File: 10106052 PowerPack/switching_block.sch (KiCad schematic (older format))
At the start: 0 parts

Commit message: start to create switching block
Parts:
- added C1, C?: 100n, symbol Device:C
- added C10, C11, C12: 10n, symbol Device:C
- added D1, D7: SMA6J28A, symbol Device:D_Schottky
- added D15: BAT54CWT1G, symbol Device:D_x2_KCom_AAK
- added D2, D8: SP0502BAHTG, symbol Device:D_Schottky_x2_ACom_KKA
- added D? (x3): PMEG4005AEA, symbol Device:D
- added J1, J2, J3, J5, J6, J7: 811-S1-002-10-015101, symbol Connector:Conn_01x02_Male
- added J4, J8: GKS 913 305 230 A 15 02 S, symbol Connector:Conn_01x01_Male
- added Q? (x2), T2, T4: SUD50P06-15, symbol Device:Q_NMOS_GDS
- added R1, R10, R7, R? (x3): 10k, symbol Device:R
- added R12, R2, R? (x2): 15k, symbol Device:R
- added R13, R8, R? (x2): 22k, symbol Device:R
- added R14, R4: 1k, symbol Device:R
- added R15 (x2): 18k, symbol Device:R
- added R28: 66.5k, symbol Device:R
- added R29: 40.2k, symbol Device:R
- added R3, R?: 100k, symbol Device:R
- added R50, R51: 100, symbol Device:R
- added R57, R58: 0, symbol Device:R
- added R?: 0.015, symbol Device:R
- added T1, T12, T13, T3, T? (x2): 2N7002TA, symbol Device:Q_NMOS_GSD
- added U3: INA170, Package_SO:MSOP-8_3x3mm_P0.65mm, symbol 10106052_PowerPack:INA170
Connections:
- new net: D1.1 (K), D?.2 (A), J1.1 (Pin_1), J1.2 (Pin_2), R2.1, R3.1, T2.3 (S)
- new net: J2.1 (Pin_1), J2.2 (Pin_2), R50.2, R57.2
- new net: D15.2 (A), R4.1, R50.1, T12.3 (D)
- new net: D2.2 (K), R57.1
- new net: D15.1 (A), R14.1, R51.1, T13.3 (D)
- new net: D7.1 (K), D?.2 (A), J5.1 (Pin_1), J5.2 (Pin_2), Q?.3 (S), R?.1, R?.1
- new net: J6.1 (Pin_1), J6.2 (Pin_2), R51.2, R58.2
- new net: D8.2 (K), R58.1
- new net: R1.2, T1.3 (D)
- new net: R1.1, R2.2, T2.1 (G)
- new net: T2.2 (D), T4.2 (D)
- new net: R10.1, R12.2, T4.1 (G)
- new net: C11.1, Q?.3 (S), R12.1, R?.1, R?.1, T4.3 (S), U3.1 (V-IN), U3.8 (V+)
- new net: R10.2, T3.3 (D)
- new net: R?.2, T?.3 (D) (x2)
- new net: Q?.1 (G), R?.1, R?.2 (x2)
- new net: Q?.2 (D), Q?.2 (D)
- new net: R?.2, U3.2 (V+IN)
- new net: R28.1, U3.5 (ROS)
- new net +3.0VREF: C10.1, U3.3 (VREF)
- new net +5V: R14.2, R15.2, R15.2, R4.2
- new net +VDC_PERM: D?.1 (K), D?.1 (K), D?.1 (K)
- new net CHARG_BAT1: R13.2, T3.1 (G)
- new net CHARG_BAT2: R?.2, T?.1 (G)
- new net DISCH_BAT1: R8.2, T1.1 (G)
- new net DISCH_BAT2: R?.2, T?.1 (G)
- new net GND: D1.2 (A), D2.3 (A), D7.2 (A), D8.3 (A), J4.1 (Pin_1), J8.1 (Pin_1), R13.1, R8.1, R?.1, R?.1, T1.2 (S), T12.2 (S), T13.2 (S), T3.2 (S), T?.2 (S), T?.2 (S)
- new net GNDA: C1.2, C10.2, C11.2, C12.2, C?.2, R28.2, R29.2, R7.2, R?.2, U3.4 (GND)
- new net IBAT_MEAS: C12.1, R29.1, U3.6 (OUT)
- new net ID_BAT1: T12.1 (G)
- new net ID_BAT2: T13.1 (G)
- new net ID_BAT_READ: D15.3 (K)
- new net TEMP_BAT1: D2.1 (K), J3.1 (Pin_1), J3.2 (Pin_2), R15.1
- new net TEMP_BAT2: D8.1 (K), J7.1 (Pin_1), J7.2 (Pin_2), R15.1
- new net VBAT1_MEAS: C1.1, R3.2, R7.1
- new net VBAT2_MEAS: C?.1, R?.1, R?.2
- new net V_DC_CHARGER: D?.2 (A)
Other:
- note added: "+BAT1"
- note added: "+BAT2"
- note added: "-BAT1"
- note added: "-BAT2"
- note added: "ID_BAT1"
- note added: "ID_BAT2"
- note added: "Note: R24 - place as close as possible to U3"

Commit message: schematic done2
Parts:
- added C14: 100n, symbol Device:C
- added C8, C?: 100u, symbol Device:CP
- added D9: SMA6J28A, symbol Device:D_Schottky
- added F1: Fuse, symbol Device:Fuse
- added FL1: BNX002-11, symbol 10106052_PowerPack:BNX002-11
- added J9: 26-61-4020, symbol Connector:Conn_01x02_Male
- added J?: 43650-0229, symbol Connector:Conn_01x02_Male
- added NT1: Net-Tie_2, symbol Device:Net-Tie_2
- added R25: 0, symbol Device:R
- added R27: 100k, symbol Device:R
- added R30, R53, R56: 10k, symbol Device:R
- added R32: 470, symbol Device:R
- added R52: 22k, symbol Device:R
- added R54: 15k, symbol Device:R
- added R55: 47k, symbol Device:R
- added RL1: 41.52.9.024.0010, Relay_THT:Relay_DPDT_Finder_40.52, symbol Relay:FINDER-41.52
- added T14: SUD50P06-15, symbol Device:Q_NMOS_GDS
- added T15: 2N7002TA, symbol Device:Q_NMOS_GSD
- gave numbers to parts that had none: 17
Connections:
- net GND: now also C8.2, C?.2, D9.2 (A), J9.2 (Pin_2), NT1.1, R52.1, R56.1, RL1.11, RL1.A2, T15.2 (S)
- net GNDA: now also C14.2, NT1.2, R30.2
- net V_DC_CHARGER: now also R25.1, R32.1
- net at R24.2, U3.2 (V+IN): now also C8.1, C?.1, R54.2, RL1.21, T14.3 (S)
- new net: FL1.1, RL1.22
- new net: FL1.2, J?.1 (Pin_1)
- new net: FL1.3, RL1.12
- new net: FL1.4, J?.2 (Pin_2)
- new net: R32.2, RL1.A1
- new net: R53.2, R54.1, T14.1 (G)
- new net: D9.1 (K), F1.1, R25.2, R27.1, R55.2, T14.2 (D)
- new net: R52.2, R55.1, R56.2, T15.1 (G)
- new net: R53.1, T15.3 (D)
- new net: F1.2, J9.1 (Pin_1)
- new net V_CH: C14.1, R27.2, R30.1
- no-connect marks 0 -> 2
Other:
- note added: "Charger DC"
- note added: "Internal battery"
- note added: "Note: J1 - J4 - TH components, place on Top side as marked;"
- note added: "Note: J5 - J8 - TH components, place on Top side as marked;"
- note added: "Note: J9 - TH component, place on Top right side;"
- note added: "Note: Join GND and AGND planes/traces;"
- note added: "Note: Power tracks (min 0.6mm, min 3.3A)\n - route as wide as possible;"
- note added: "Note: RL1, FL1 & J11 - TH components, place on Top right side;"
- note added: "Removable battery"
- note added: "TEMP_BAT1"
- note added: "TEMP_BAT2"
- moved on the sheet: C1, C10, C11, C12, C4, D1, D15, D2, D3, D4, D6, D7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

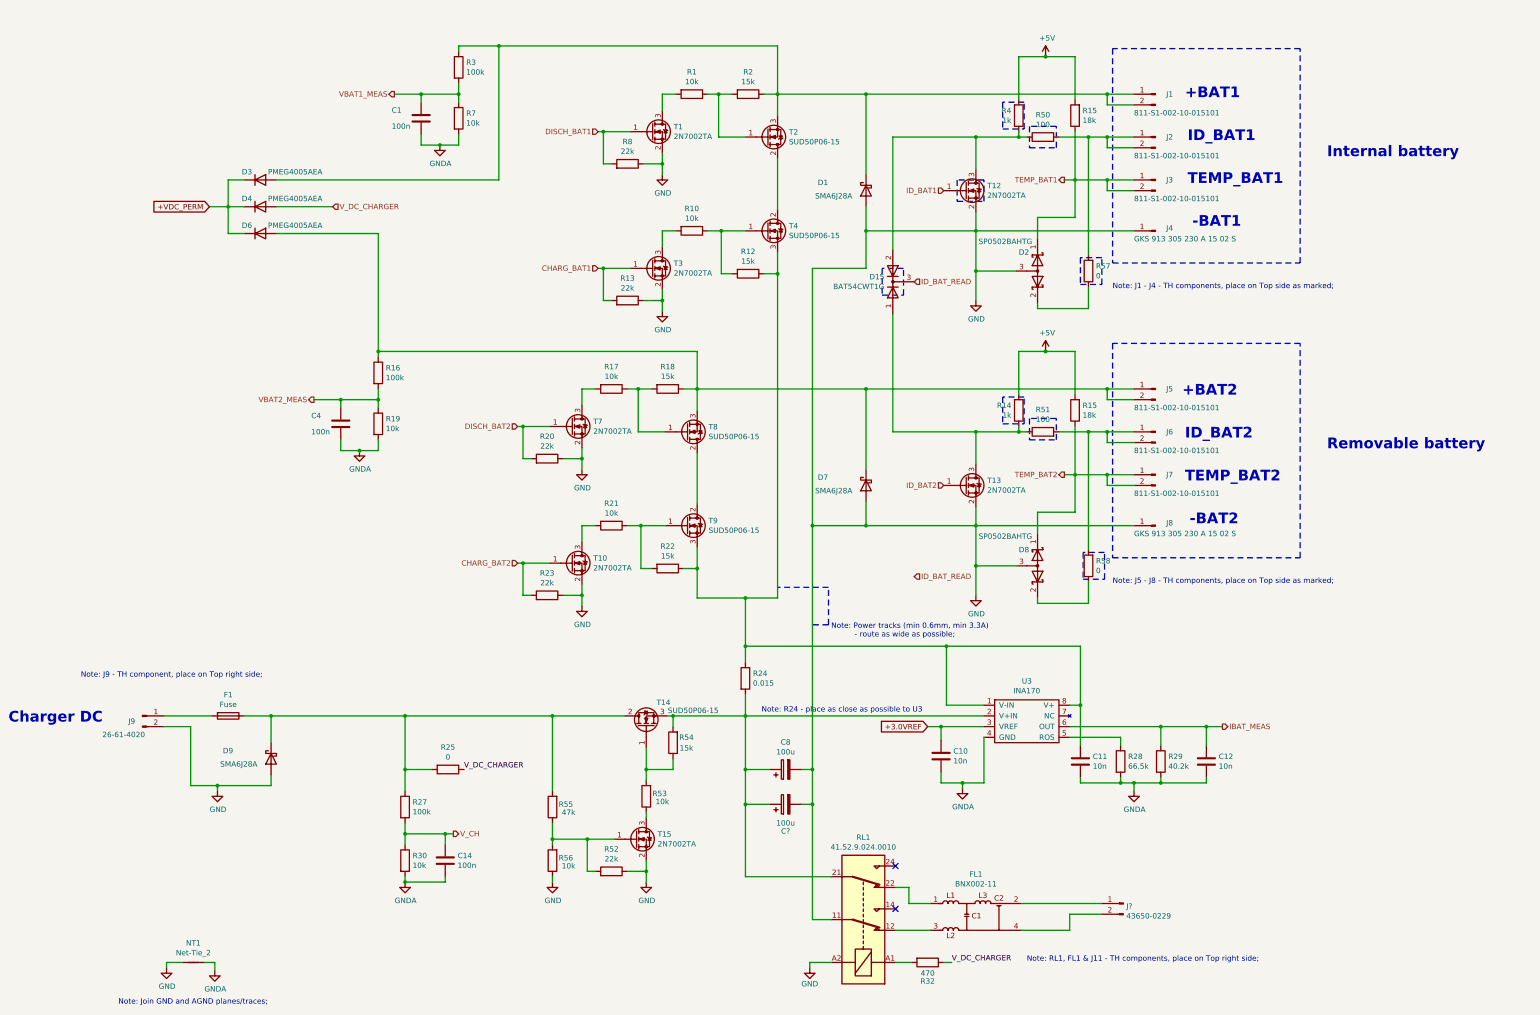
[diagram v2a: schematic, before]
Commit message: PowerPack schematic toplevel done
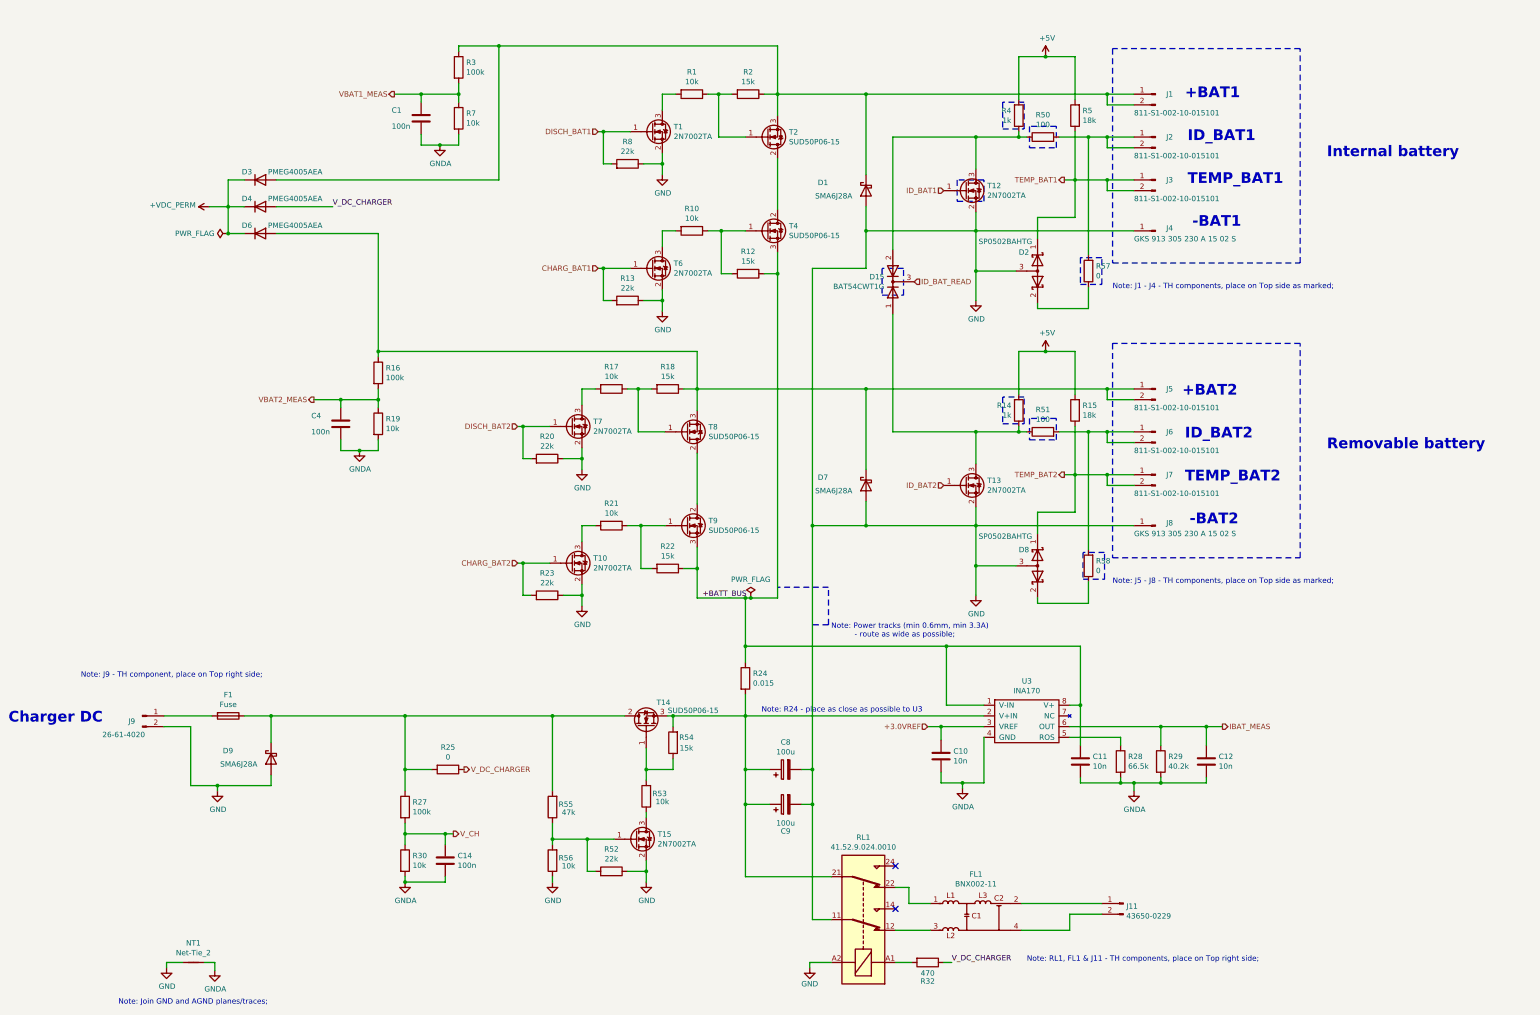
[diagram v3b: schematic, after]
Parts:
- gave numbers to parts that had none: 2
- renumbered R15 to R5, T3 to T6
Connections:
- net +BATT_BUS: now reaches C11.1, R12.1, R22.1, R24.1, T4.3 (S), T9.3 (S), U3.1 (V-IN), U3.8 (V+)
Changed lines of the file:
@@
 $Descr A3 16535 11693
 encoding utf-8
-Sheet 2 7
+Sheet 2 4
 Title "Switching block"
 Date "2020-04-04"
@@
 $EndComp
 $Comp
-L Device:R R15
+L Device:R R5
 U 1 1 5E8871D7
 P 10650 1625
-F 0 "R15" H 10580 1579 50  0000 R CNN
+F 0 "R5" H 10580 1579 50  0000 R CNN
 F 1 "18k" H 10580 1670 50  0000 R CNN
 F 2 "" V 10580 1625 50  0001 C CNN
@@
 	10125 1075 10125 1475
 $Comp
-L power:+5V #PWR?
+L power:+5V #PWR0101
 U 1 1 5E889F59
 P 10375 1075
-F 0 "#PWR?" H 10375 925 50  0001 C CNN
+F 0 "#PWR0101" H 10375 925 50  0001 C CNN
 F 1 "+5V" H 10390 1248 50  0000 C CNN
 F 2 "" H 10375 1075 50  0001 C CNN
@@
 	9725 2700 9725 3075
 $Comp
-L power:GND #PWR?
+L power:GND #PWR0102
 U 1 1 5E88E772
 P 9725 3350
-F 0 "#PWR?" H 9725 3100 50  0001 C CNN
+F 0 "#PWR0102" H 9725 3100 50  0001 C CNN
 F 1 "GND" H 9730 3177 50  0000 C CNN
 F 2 "" H 9725 3350 50  0001 C CNN
@@
 	10125 3825 10125 4225
 $Comp
-L power:+5V #PWR?
+L power:+5V #PWR0103
 U 1 1 5E8B3A3A
 P 10375 3825
-F 0 "#PWR?" H 10375 3675 50  0001 C CNN
+F 0 "#PWR0103" H 10375 3675 50  0001 C CNN
 F 1 "+5V" H 10390 3998 50  0000 C CNN
 F 2 "" H 10375 3825 50  0001 C CNN
@@
 	9725 5450 9725 5825
 $Comp
-L power:GND #PWR?
+L power:GND #PWR0104
 U 1 1 5E8B3A59
 P 9725 6100
-F 0 "#PWR?" H 9725 5850 50  0001 C CNN
+F 0 "#PWR0104" H 9725 5850 50  0001 C CNN
 F 1 "GND" H 9730 5927 50  0000 C CNN
 F 2 "" H 9725 6100 50  0001 C CNN
@@
 Text HLabel 9425 5075 0    50   Input ~ 0
 ID_BAT2
-Text HLabel 9150 5925 2    50   Input ~ 0
-ID_BAT_READ
 $Comp
 L Device:D_Schottky D7
@@
 DISCH_BAT1
 $Comp
-L power:GND #PWR?
+L power:GND #PWR0105
 U 1 1 5E9062A8
 P 6800 2175
-F 0 "#PWR?" H 6800 1925 50  0001 C CNN
+F 0 "#PWR0105" H 6800 1925 50  0001 C CNN
 F 1 "GND" H 6805 2002 50  0000 C CNN
 F 2 "" H 6800 2175 50  0001 C CNN
@@
 $EndComp
 $Comp
-L Device:Q_NMOS_GSD T3
+L Device:Q_NMOS_GSD T6
 U 1 1 5E90AD6B
 P 6700 3050
-F 0 "T3" H 6906 3096 50  0000 L CNN
+F 0 "T6" H 6906 3096 50  0000 L CNN
 F 1 "2N7002TA" H 6906 3005 50  0000 L CNN
 F 2 "" H 6900 3150 50  0001 C CNN
@@
 CHARG_BAT1
 $Comp
-L power:GND #PWR?
+L power:GND #PWR0106
 U 1 1 5E90AD94
 P 6800 3450
-F 0 "#PWR?" H 6800 3200 50  0001 C CNN
+F 0 "#PWR0106" H 6800 3200 50  0001 C CNN
 F 1 "GND" H 6805 3277 50  0000 C CNN
 F 2 "" H 6800 3450 50  0001 C CNN
@@
 DISCH_BAT2
 $Comp
-L power:GND #PWR?
+L power:GND #PWR0107
 U 1 1 5E94B709
 P 6050 4925
-F 0 "#PWR?" H 6050 4675 50  0001 C CNN
+F 0 "#PWR0107" H 6050 4675 50  0001 C CNN
 F 1 "GND" H 6055 4752 50  0000 C CNN
 F 2 "" H 6050 4925 50  0001 C CNN
@@
 CHARG_BAT2
 $Comp
-L power:GND #PWR?
+L power:GND #PWR0108
 U 1 1 5E94B737
 P 6050 6200
-F 0 "#PWR?" H 6050 5950 50  0001 C CNN
+F 0 "#PWR0108" H 6050 5950 50  0001 C CNN
 F 1 "GND" H 6055 6027 50  0000 C CNN
 F 2 "" H 6050 6200 50  0001 C CNN
@@
 	8200 3050 8200 5450
 Wire Wire Line
-	7875 6125 7575 6125
+	7875 6125 7625 6125
 Wire Wire Line
 	7875 3100 7875 6125
@@
 $EndComp
 $Comp
-L power:GNDA #PWR?
+L power:GNDA #PWR0109
 U 1 1 5E98B385
 P 4725 1900
-F 0 "#PWR?" H 4725 1650 50  0001 C CNN
+F 0 "#PWR0109" H 4725 1650 50  0001 C CNN
 F 1 "GNDA" H 4730 1727 50  0000 C CNN
 F 2 "" H 4725 1900 50  0001 C CNN
@@
 $EndComp
 $Comp
-L power:GNDA #PWR?
+L power:GNDA #PWR0110
 U 1 1 5E9D793F
 P 3975 4750
-F 0 "#PWR?" H 3975 4500 50  0001 C CNN
+F 0 "#PWR0110" H 3975 4500 50  0001 C CNN
 F 1 "GNDA" H 3980 4577 50  0000 C CNN
 F 2 "" H 3975 4750 50  0001 C CNN
@@
 Wire Wire Line
 	3200 2475 3725 2475
-Text HLabel 3725 2475 2    50   Input ~ 0
+Text HLabel 4950 7725 2    50   Output ~ 0
 V_DC_CHARGER
 Wire Wire Line
@@
 Wire Wire Line
 	2750 2475 2575 2475
-Text GLabel 2575 2475 0    50   Input ~ 0
-+VDC_PERM
 $Comp
 L 10106052_PowerPack:INA170 U3
@@
 	9600 7850 9400 7850
 $Comp
-L power:GNDA #PWR?
+L power:GNDA #PWR0111
 U 1 1 5EB09572
 P 9600 7900
-F 0 "#PWR?" H 9600 7650 50  0001 C CNN
+F 0 "#PWR0111" H 9600 7650 50  0001 C CNN
 F 1 "GNDA" H 9605 7727 50  0000 C CNN
 F 2 "" H 9600 7900 50  0001 C CNN
@@
 	1    0    0    -1
 $EndComp
-Text GLabel 9275 7325 0    50   Input ~ 0
-+3.0VREF
 $Comp
 L Device:C C11
@@
 	11200 7850 11450 7850
 $Comp
-L power:GNDA #PWR?
+L power:GNDA #PWR0112
 U 1 1 5EBA12AC
 P 11200 7925
-F 0 "#PWR?" H 11200 7675 50  0001 C CNN
+F 0 "#PWR0112" H 11200 7675 50  0001 C CNN
 F 1 "GNDA" H 11205 7752 50  0000 C CNN
 F 2 "" H 11200 7925 50  0001 C CNN
@@
 $EndComp
 $Comp
-L Connector:Conn_01x02_Male J?
+L Connector:Conn_01x02_Male J11
 U 1 1 5E898ED2
 P 11100 8975
-F 0 "J?" H 11072 8949 50  0000 R CNN
+F 0 "J11" H 11072 8949 50  0000 R CNN
 F 1 "43650-0229" H 11072 8858 50  0000 R CNN
 F 2 "" H 11100 8975 50  0001 C CNN
@@
 	9100 8975 9300 8975
 $Comp
-L power:GND #PWR?
+L power:GND #PWR0113
 U 1 1 5E94404C
 P 8175 9575
-F 0 "#PWR?" H 8175 9325 50  0001 C CNN
+F 0 "#PWR0113" H 8175 9325 50  0001 C CNN
 F 1 "GND" H 8175 9425 50  0000 C CNN
 F 2 "" H 8175 9575 50  0001 C CNN
@@
 $EndComp
 $Comp
-L Device:CP C?
+L Device:CP C9
 U 1 1 5EA29795
 P 7950 8050
-F 0 "C?" V 7700 8050 50  0000 C CNN
+F 0 "C9" V 7700 8050 50  0000 C CNN
 F 1 "100u" V 7775 8050 50  0000 C CNN
 F 2 "" H 7988 7900 50  0001 C CNN
@@
 Connection ~ 6100 8375
 $Comp
-L power:GND #PWR?
+L power:GND #PWR0114
 U 1 1 5EAD2184
 P 6650 8775
-F 0 "#PWR?" H 6650 8525 50  0001 C CNN
+F 0 "#PWR0114" H 6650 8525 50  0001 C CNN
 F 1 "GND" H 6655 8602 50  0000 C CNN
 F 2 "" H 6650 8775 50  0001 C CNN
@@
 	5775 8375 5775 8225
 $Comp
-L power:GND #PWR?
+L power:GND #PWR0115
 U 1 1 5EC2D61C
 P 5775 8775
-F 0 "#PWR?" H 5775 8525 50  0001 C CNN
+F 0 "#PWR0115" H 5775 8525 50  0001 C CNN
 F 1 "GND" H 5780 8602 50  0000 C CNN
 F 2 "" H 5775 8775 50  0001 C CNN
@@
 $EndComp
 $Comp
-L power:GND #PWR?
+L power:GND #PWR0116
 U 1 1 5EC49419
 P 2175 9575
-F 0 "#PWR?" H 2175 9325 50  0001 C CNN
+F 0 "#PWR0116" H 2175 9325 50  0001 C CNN
 F 1 "GND" H 2180 9402 50  0000 C CNN
 F 2 "" H 2175 9575 50  0001 C CNN
@@
 	2625 9525 2625 9600
 $Comp
-L power:GNDA #PWR?
+L power:GNDA #PWR0117
 U 1 1 5EC7777C
 P 2625 9600
-F 0 "#PWR?" H 2625 9350 50  0001 C CNN
+F 0 "#PWR0117" H 2625 9350 50  0001 C CNN
 F 1 "GNDA" H 2630 9427 50  0000 C CNN
 F 2 "" H 2625 9600 50  0001 C CNN
@@
 	4400 8725 4400 8775
 $Comp
-L power:GNDA #PWR?
+L power:GNDA #PWR0118
 U 1 1 5ED0A6F1
 P 4400 8775
-F 0 "#PWR?" H 4400 8525 50  0001 C CNN
+F 0 "#PWR0118" H 4400 8525 50  0001 C CNN
 F 1 "GNDA" H 4405 8602 50  0000 C CNN
 F 2 "" H 4400 8775 50  0001 C CNN
@@
 Connection ~ 4775 8325
 Text Label 9500 9525 0    50   ~ 0
-V_DC_CHARGER
-Text Label 4950 7725 0    50   ~ 0
 V_DC_CHARGER
 $Comp
@@
 	2650 7875 2650 7925
 $Comp
-L power:GND #PWR?
+L power:GND #PWR0119
 U 1 1 5EFACD0C
 P 2650 7925
-F 0 "#PWR?" H 2650 7675 50  0001 C CNN
+F 0 "#PWR0119" H 2650 7675 50  0001 C CNN
 F 1 "GND" H 2655 7752 50  0000 C CNN
 F 2 "" H 2650 7925 50  0001 C CNN
@@
 Text Notes 10200 9525 0    50   ~ 0
 Note: RL1, FL1 & J11 - TH components, place on Top right side;
+$Comp
+L 10106052_PowerPack:+VDC_PERM #PWR0120
+U 1 1 5E8C661B
+P 2575 2475
+F 0 "#PWR0120" H 2575 2325 50  0001 C CNN
+F 1 "+VDC_PERM" V 2590 2602 50  0000 L CNN
+F 2 "" H 2575 2475 50  0001 C CNN
+F 3 "" H 2575 2475 50  0001 C CNN
+	1    2575 2475
+	0    -1   -1   0
+$EndComp
+Text HLabel 9275 7325 0    50   Input ~ 0
++3.0VREF
+Text Label 3725 2475 0    50   ~ 0
+V_DC_CHARGER
+Text Label 7175 6125 0    50   ~ 0
++BATT_BUS
+$Comp
+L power:PWR_FLAG #FLG0103
+U 1 1 5E9783CF
+P 7625 6125
+F 0 "#FLG0103" H 7625 6200 50  0001 C CNN
+F 1 "PWR_FLAG" H 7625 6298 50  0000 C CNN
+F 2 "" H 7625 6125 50  0001 C CNN
+F 3 "~" H 7625 6125 50  0001 C CNN
+	1    7625 6125
+	1    0    0    -1
+$EndComp
+Connection ~ 7625 6125
+Wire Wire Line
+	7625 6125 7575 6125
+$Comp
+L power:PWR_FLAG #FLG0104
+U 1 1 5E97BAC7
+P 2750 2725
+F 0 "#FLG0104" H 2750 2800 50  0001 C CNN
+F 1 "PWR_FLAG" V 2750 2852 50  0000 L CNN
+F 2 "" H 2750 2725 50  0001 C CNN
+F 3 "~" H 2750 2725 50  0001 C CNN
+	1    2750 2725
+	0    -1   -1   0
+$EndComp
+Connection ~ 2750 2725
 $EndSCHEMATC

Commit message: PCB Added and Schematic Footprints Added
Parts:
- C1, C10, C11, C12, C14, C4: footprint (none) -> Capacitor_SMD:C_0603_1608Metric
- C8, C9: footprint (none) -> Capacitor_THT:CP_Radial_D8.0mm_P3.50mm
- D1, D7, D9: footprint (none) -> Diode_SMD:D_SMA
- D15, D2, D8: footprint (none) -> Package_TO_SOT_SMD:SOT-323_SC-70
- D3, D4, D6: footprint (none) -> Diode_SMD:D_SOD-323
- J1, J2, J3, J5, J6, J7: footprint (none) -> Connector_PinHeader_2.54mm:PinHeader_1x02_P2.54mm_Vertical
- R1, R10, R12, R13, R14, R15, R16, R17, R18, R19, R2, R20, R21, R22, R23, R27, R28, R29, R3, R30, R4, R5, R50, R51, R52, R53, R54, R55, R56, R57, R58, R7, R8: footprint (none) -> Resistor_SMD:R_0603_1608Metric
- R24: footprint (none) -> Resistor_SMD:R_2512_6332Metric
- R25, R32: footprint (none) -> Resistor_SMD:R_1206_3216Metric
- T1, T10, T12, T13, T15, T6, T7: footprint (none) -> Package_TO_SOT_SMD:SOT-23
- T14, T2, T4, T8, T9: footprint (none) -> Package_TO_SOT_SMD:TO-252-3_TabPin2
